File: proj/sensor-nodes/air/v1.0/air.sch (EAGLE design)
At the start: 68 parts, among them J1 54602-908LF, J2 54602-908LF, U2 PCA9615DPJ, U3 MIC4680YM-TR, U4 LM2937IMP3.3NOPB, U5 SHT25, U6 CCS811, U7 T6713-5K, U8 HPP845E034R5

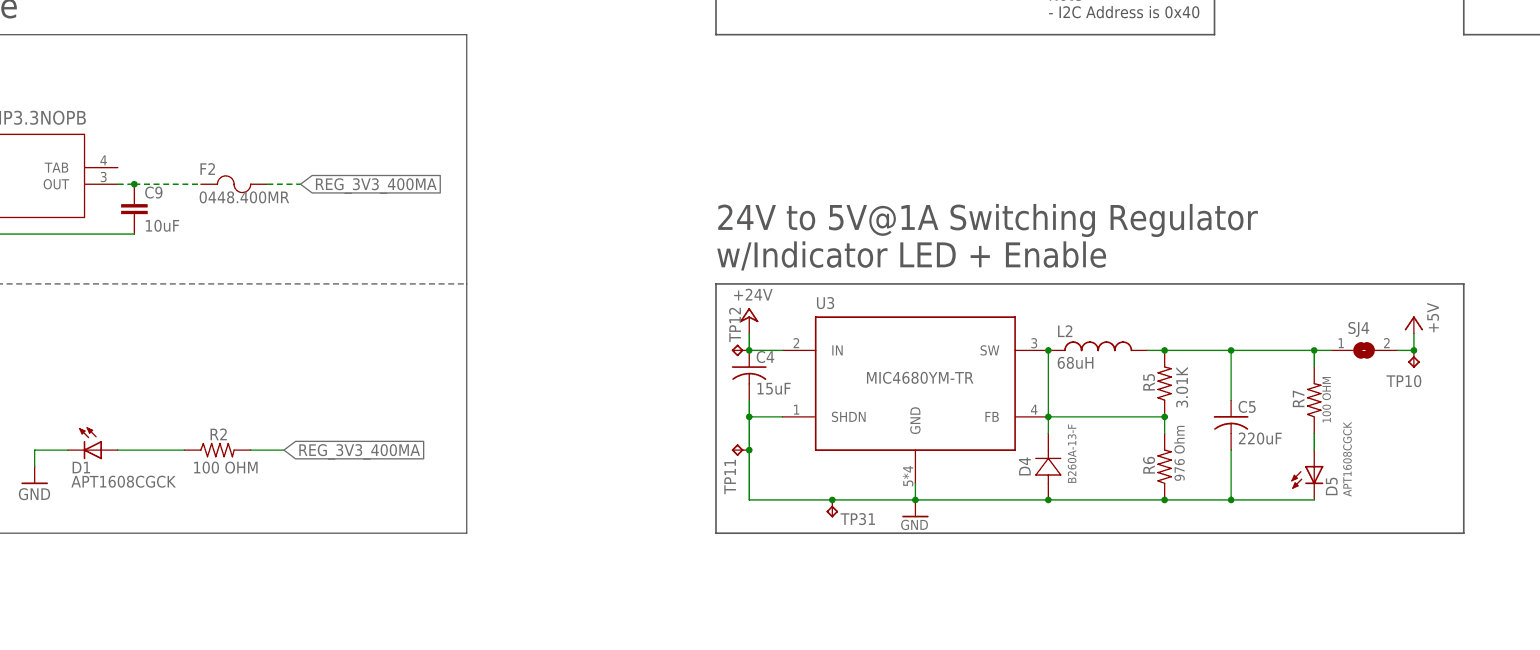
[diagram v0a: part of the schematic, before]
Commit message: minor changes to air sensor node after design review
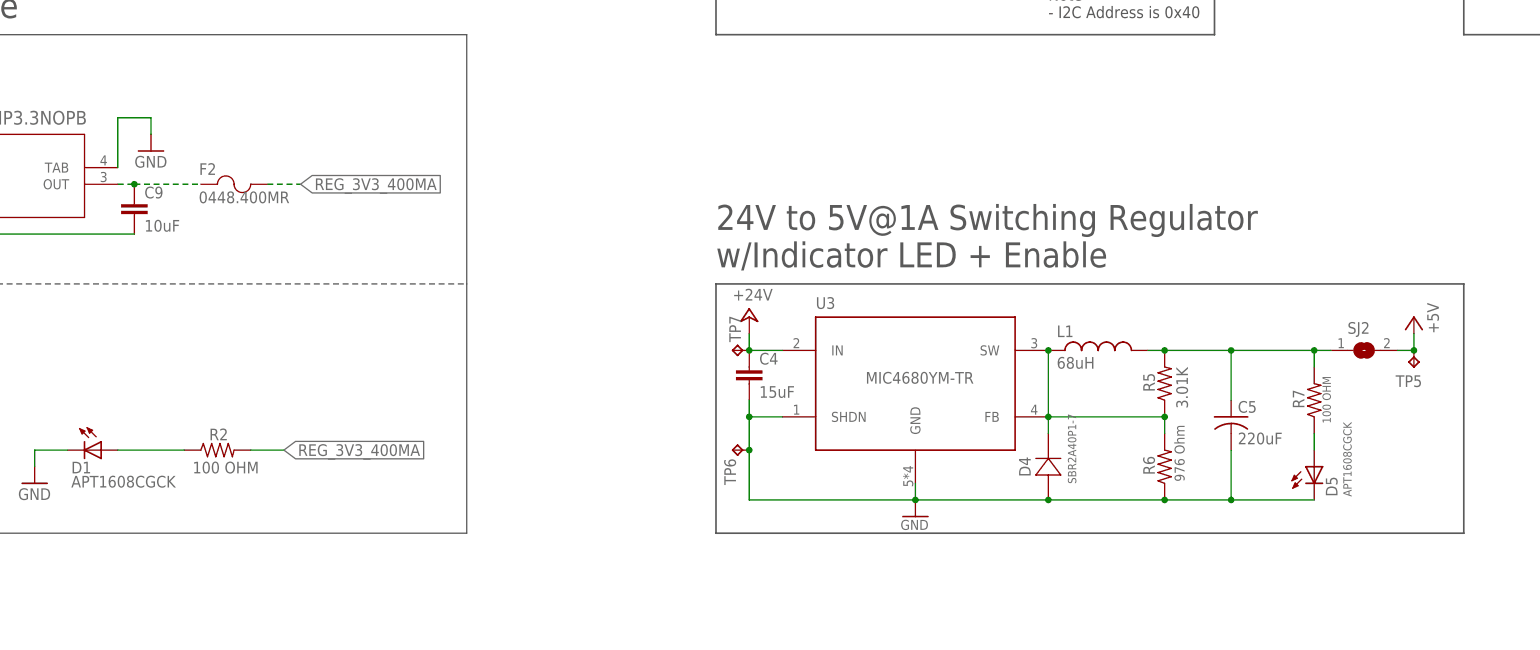
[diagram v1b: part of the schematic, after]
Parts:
- removed TP31: TPTP06R, openag-testpads:TPTP06R
- C4: device openag-capacitors:15UF-TPSD156K035R0100 -> openag-capacitors:15UF-C2012X5R1V156M125AC
- D4: value B260A-13-F -> SBR2A40P1-7; device openag-diodes:B260A-13-F -> openag-diodes:SBR2A40P1-7
- renumbered L2 to L1, SJ4 to SJ2, TP10 to TP5, TP11 to TP6, TP12 to TP7
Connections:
- net +24V: now also C4.1; no longer C4.1(+)
- net GND: now also C4.2, U4.TAB; no longer C4.2(-), TP31.TP
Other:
- note added: "3.3V@400mA Regulator"
- note removed: "3.3V, 400mA Regulator"

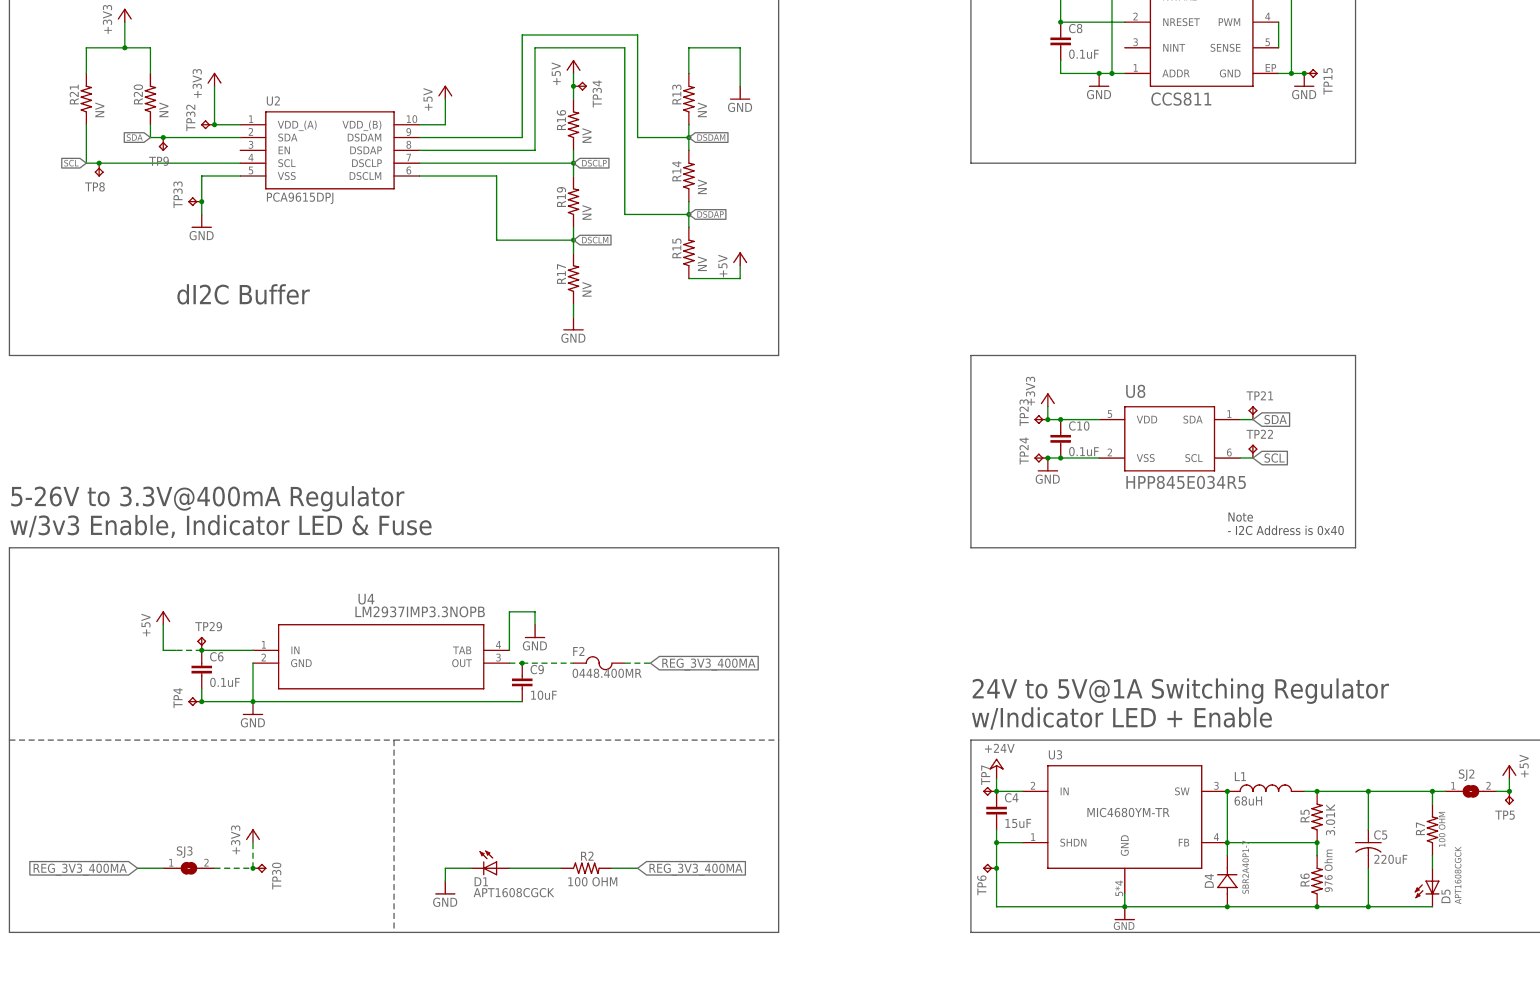
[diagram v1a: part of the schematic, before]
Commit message: added light and rj12 nodes, started working on light controller v2
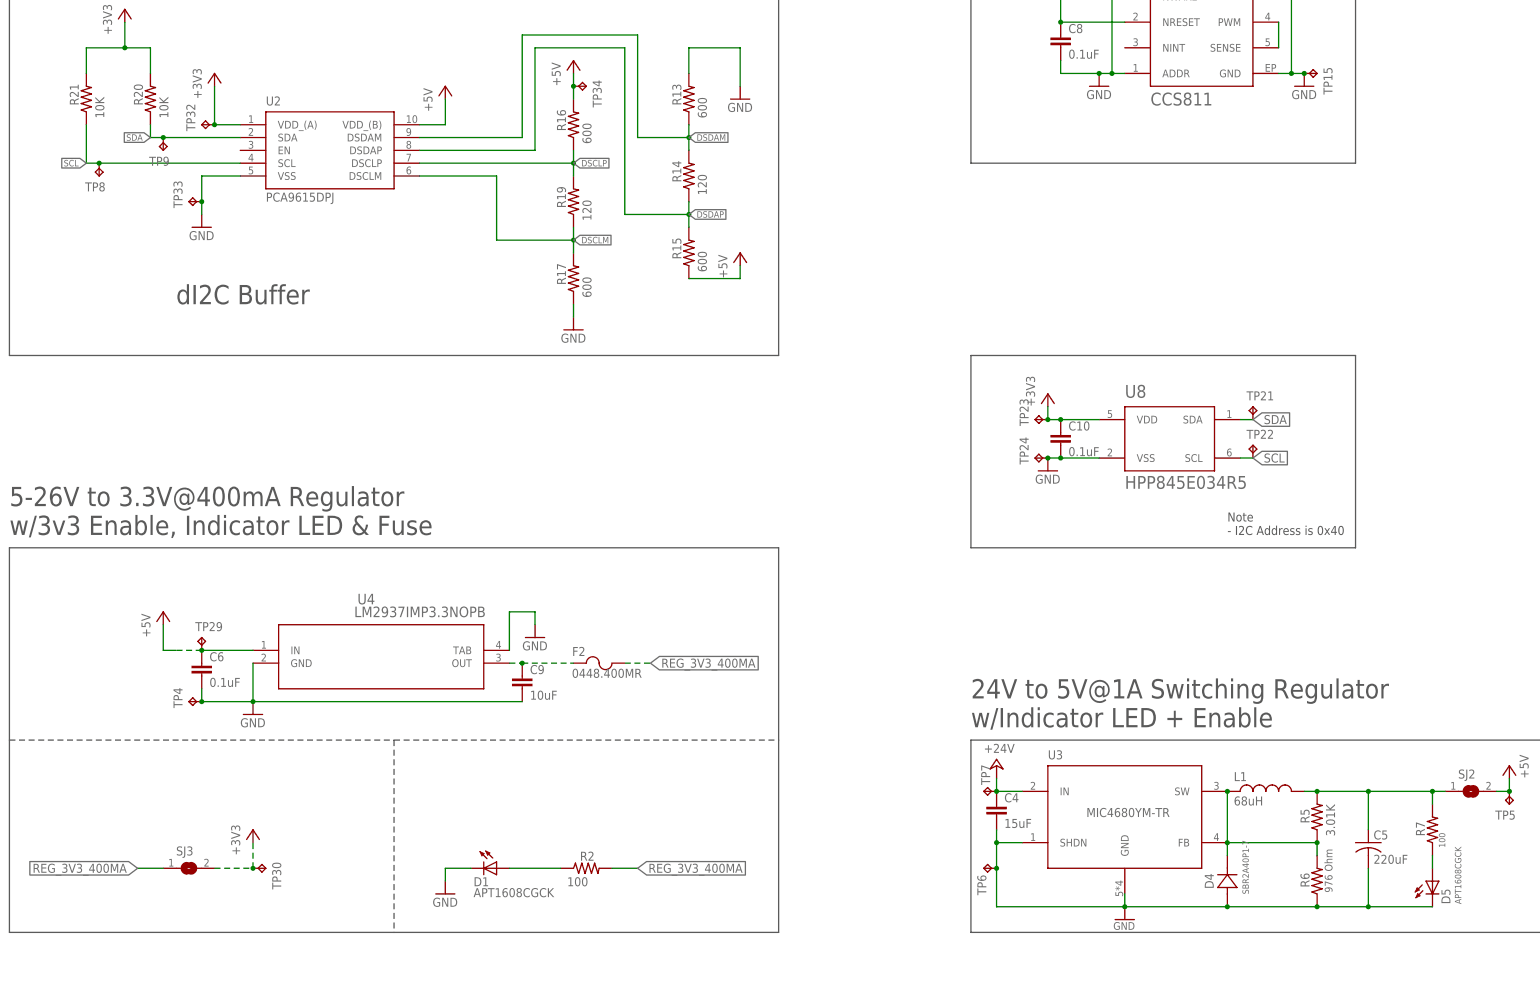
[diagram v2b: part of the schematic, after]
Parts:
- R13, R15, R16, R17: value NV -> 600; device openag-resistors:R0603 -> openag-resistors:600OHM-RC0603FR-07604RL
- R14, R19: value NV -> 120; device openag-resistors:R0603 -> openag-resistors:120OHM-RC0603FR-07120RL
- R2, R7: value 100 OHM -> 100
- R20, R21: value NV -> 10K; device openag-resistors:R0603 -> openag-resistors:10K-ERJ-3EKF1002V
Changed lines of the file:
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@@
 <setting verticaltext="up"/>
 </settings>
-<grid distance="0.1" unitdist="inch" unit="inch" style="lines" multiple="1" display="yes" altdistance="0.01" altunitdist="inch" altunit="inch"/>
+<grid distance="1.5" unitdist="inch" unit="inch" style="lines" multiple="1" display="yes" altdistance="0.01" altunitdist="inch" altunit="inch"/>
 <layers>
 <layer number="1" name="Top" color="4" fill="1" visible="no" active="no"/>
@@
 </part>
 <part name="D1" library="openag-diodes" deviceset="APT1608CGCK" device="" value="APT1608CGCK"/>
-<part name="R2" library="openag-resistors" deviceset="100OHM-RC0603JR-07100RL" device="" value="100 OHM"/>
+<part name="R2" library="openag-resistors" deviceset="100OHM-RC0603JR-07100RL" device="" value="100"/>
 <part name="GND5" library="openag-supply" deviceset="GND" device=""/>
 <part name="U4" library="openag-regulators" deviceset="LM2937IMP-3.3/NOPB" device="" value="LM2937IMP3.3NOPB"/>
@@
 <part name="P+1" library="openag-supply" deviceset="+5V" device=""/>
 <part name="U2" library="openag-buffers" deviceset="PCA9615DPJ" device="" value="PCA9615DPJ"/>
-<part name="R13" library="openag-resistors" deviceset="R0603" device="" value="NV"/>
-<part name="R14" library="openag-resistors" deviceset="R0603" device="" value="NV"/>
-<part name="R15" library="openag-resistors" deviceset="R0603" device="" value="NV"/>
-<part name="R16" library="openag-resistors" deviceset="R0603" device="" value="NV"/>
+<part name="R13" library="openag-resistors" deviceset="600OHM-RC0603FR-07604RL" device="" value="600"/>
+<part name="R14" library="openag-resistors" deviceset="120OHM-RC0603FR-07120RL" device="" value="120"/>
+<part name="R15" library="openag-resistors" deviceset="600OHM-RC0603FR-07604RL" device="" value="600"/>
+<part name="R16" library="openag-resistors" deviceset="600OHM-RC0603FR-07604RL" device="" value="600"/>
 <part name="+3V4" library="openag-supply" deviceset="+3V3" device=""/>
 <part name="P+8" library="openag-supply" deviceset="+24V" device=""/>
@@
 <part name="GND10" library="openag-supply" deviceset="GND" device=""/>
 <part name="GND15" library="openag-supply" deviceset="GND" device=""/>
-<part name="R17" library="openag-resistors" deviceset="R0603" device="" value="NV"/>
-<part name="R19" library="openag-resistors" deviceset="R0603" device="" value="NV"/>
+<part name="R17" library="openag-resistors" deviceset="600OHM-RC0603FR-07604RL" device="" value="600"/>
+<part name="R19" library="openag-resistors" deviceset="120OHM-RC0603FR-07120RL" device="" value="120"/>
 <part name="GND17" library="openag-supply" deviceset="GND" device=""/>
-<part name="R20" library="openag-resistors" deviceset="R0603" device="" value="NV"/>
-<part name="R21" library="openag-resistors" deviceset="R0603" device="" value="NV"/>
+<part name="R20" library="openag-resistors" deviceset="10K-ERJ-3EKF1002V" device="" value="10K"/>
+<part name="R21" library="openag-resistors" deviceset="10K-ERJ-3EKF1002V" device="" value="10K"/>
 <part name="+3V9" library="openag-supply" deviceset="+3V3" device=""/>
 <part name="P+9" library="openag-supply" deviceset="+5V" device=""/>
@@
 <part name="P+4" library="openag-supply" deviceset="+24V" device=""/>
 <part name="P+5" library="openag-supply" deviceset="+5V" device=""/>
-<part name="R7" library="openag-resistors" deviceset="100OHM-RC0603JR-07100RL" device="" value="100 OHM"/>
+<part name="R7" library="openag-resistors" deviceset="100OHM-RC0603JR-07100RL" device="" value="100"/>
 <part name="D5" library="openag-diodes" deviceset="APT1608CGCK" device="" value="APT1608CGCK"/>
 <part name="TP5" library="openag-testpads" deviceset="TP" device="TP06R"/>
@@
 <instance part="P+1" gate="1" x="-121.92" y="-12.7"/>
 <instance part="U2" gate="G$1" x="-88.9" y="78.74"/>
-<instance part="R13" gate="1" x="-17.78" y="88.9" rot="R90"/>
-<instance part="R14" gate="1" x="-17.78" y="73.66" rot="R90"/>
-<instance part="R15" gate="1" x="-17.78" y="58.42" rot="R90"/>
-<instance part="R16" gate="1" x="-40.64" y="83.82" rot="R90"/>
+<instance part="R13" gate="G$1" x="-17.78" y="88.9" rot="R90"/>
+<instance part="R14" gate="G$1" x="-17.78" y="73.66" rot="R90"/>
+<instance part="R15" gate="G$1" x="-17.78" y="58.42" rot="R90"/>
+<instance part="R16" gate="G$1" x="-40.64" y="83.82" rot="R90"/>
 <instance part="+3V4" gate="G$1" x="-111.76" y="93.98"/>
 <instance part="P+8" gate="1" x="-134.62" y="142.24"/>
@@
 <instance part="GND10" gate="1" x="-129.54" y="116.84"/>
 <instance part="GND15" gate="1" x="-7.62" y="88.9"/>
-<instance part="R17" gate="1" x="-40.64" y="53.34" rot="R90"/>
-<instance part="R19" gate="1" x="-40.64" y="68.58" rot="R90"/>
+<instance part="R17" gate="G$1" x="-40.64" y="53.34" rot="R90"/>
+<instance part="R19" gate="G$1" x="-40.64" y="68.58" rot="R90"/>
 <instance part="GND17" gate="1" x="-40.64" y="43.18"/>
-<instance part="R20" gate="1" x="-124.46" y="88.9" rot="R90"/>
-<instance part="R21" gate="1" x="-137.16" y="88.9" rot="R90"/>
+<instance part="R20" gate="A" x="-124.46" y="88.9" rot="R90"/>
+<instance part="R21" gate="A" x="-137.16" y="88.9" rot="R90"/>
 <instance part="+3V9" gate="G$1" x="-129.54" y="106.68"/>
 <instance part="P+9" gate="1" x="-66.04" y="91.44"/>
@@
 </segment>
 <segment>
-<pinref part="R13" gate="1" pin="2"/>
+<pinref part="R13" gate="G$1" pin="2"/>
 <wire x1="-17.78" y1="93.98" x2="-17.78" y2="99.06" width="0.1524" layer="91"/>
 <wire x1="-17.78" y1="99.06" x2="-7.62" y2="99.06" width="0.1524" layer="91"/>
@@
 </segment>
 <segment>
-<pinref part="R17" gate="1" pin="1"/>
+<pinref part="R17" gate="G$1" pin="1"/>
 <pinref part="GND17" gate="1" pin="GND"/>
 <wire x1="-40.64" y1="48.26" x2="-40.64" y2="45.72" width="0.1524" layer="91"/>
@@
 <segment>
 <pinref part="U2" gate="G$1" pin="SCL"/>
-<pinref part="R21" gate="1" pin="1"/>
+<pinref part="R21" gate="A" pin="1"/>
 <wire x1="-106.68" y1="76.2" x2="-134.62" y2="76.2" width="0.1524" layer="91"/>
 <wire x1="-134.62" y1="76.2" x2="-137.16" y2="76.2" width="0.1524" layer="91"/>
@@
 </segment>
 <segment>
-<pinref part="R20" gate="1" pin="1"/>
+<pinref part="R20" gate="A" pin="1"/>
 <wire x1="-124.46" y1="83.82" x2="-124.46" y2="81.28" width="0.1524" layer="91"/>
 <pinref part="U2" gate="G$1" pin="SDA"/>
@@
 </segment>
 <segment>
-<pinref part="R21" gate="1" pin="2"/>
+<pinref part="R21" gate="A" pin="2"/>
 <wire x1="-137.16" y1="93.98" x2="-137.16" y2="99.06" width="0.1524" layer="91"/>
 <wire x1="-137.16" y1="99.06" x2="-129.54" y2="99.06" width="0.1524" layer="91"/>
-<pinref part="R20" gate="1" pin="2"/>
+<pinref part="R20" gate="A" pin="2"/>
 <wire x1="-129.54" y1="99.06" x2="-124.46" y2="99.06" width="0.1524" layer="91"/>
 <wire x1="-124.46" y1="99.06" x2="-124.46" y2="93.98" width="0.1524" layer="91"/>
@@
 </segment>
 <segment>
-<pinref part="R16" gate="1" pin="2"/>
+<pinref part="R16" gate="G$1" pin="2"/>
 <wire x1="-40.64" y1="93.98" x2="-40.64" y2="91.44" width="0.1524" layer="91"/>
 <pinref part="P+10" gate="1" pin="+5V"/>
@@
 </segment>
 <segment>
-<pinref part="R15" gate="1" pin="1"/>
+<pinref part="R15" gate="G$1" pin="1"/>
 <wire x1="-17.78" y1="53.34" x2="-7.62" y2="53.34" width="0.1524" layer="91"/>
 <wire x1="-7.62" y1="53.34" x2="-7.62" y2="55.88" width="0.1524" layer="91"/>
@@
 <net name="DSDAM" class="0">
 <segment>
-<pinref part="R13" gate="1" pin="1"/>
-<pinref part="R14" gate="1" pin="2"/>
+<pinref part="R13" gate="G$1" pin="1"/>
+<pinref part="R14" gate="G$1" pin="2"/>
 <wire x1="-17.78" y1="78.74" x2="-17.78" y2="81.28" width="0.1524" layer="91"/>
 <label x="-17.78" y="81.28" size="1.27" layer="95" xref="yes"/>
@@
 <net name="DSDAP" class="0">
 <segment>
-<pinref part="R14" gate="1" pin="1"/>
-<pinref part="R15" gate="1" pin="2"/>
+<pinref part="R14" gate="G$1" pin="1"/>
+<pinref part="R15" gate="G$1" pin="2"/>
 <wire x1="-17.78" y1="68.58" x2="-17.78" y2="66.04" width="0.1524" layer="91"/>
 <wire x1="-17.78" y1="66.04" x2="-17.78" y2="63.5" width="0.1524" layer="91"/>
@@
 <net name="DSCLP" class="0">
 <segment>
-<pinref part="R16" gate="1" pin="1"/>
-<pinref part="R19" gate="1" pin="2"/>
+<pinref part="R16" gate="G$1" pin="1"/>
+<pinref part="R19" gate="G$1" pin="2"/>
 <wire x1="-40.64" y1="78.74" x2="-40.64" y2="76.2" width="0.1524" layer="91"/>
 <pinref part="U2" gate="G$1" pin="DSCLP"/>
@@
 <net name="DSCLM" class="0">
 <segment>
-<pinref part="R19" gate="1" pin="1"/>
-<pinref part="R17" gate="1" pin="2"/>
+<pinref part="R19" gate="G$1" pin="1"/>
+<pinref part="R17" gate="G$1" pin="2"/>
 <wire x1="-40.64" y1="63.5" x2="-40.64" y2="60.96" width="0.1524" layer="91"/>
 <pinref part="U2" gate="G$1" pin="DSCLM"/>
